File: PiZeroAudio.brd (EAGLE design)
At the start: 65.1 x 30.2 mm, 53 parts, among them CN1 1X4-BIG, CON1 RPI-ZERO, J1 1X2-3.5MM, U3 NC7WZ16, U4 TPA3144D2PWPR

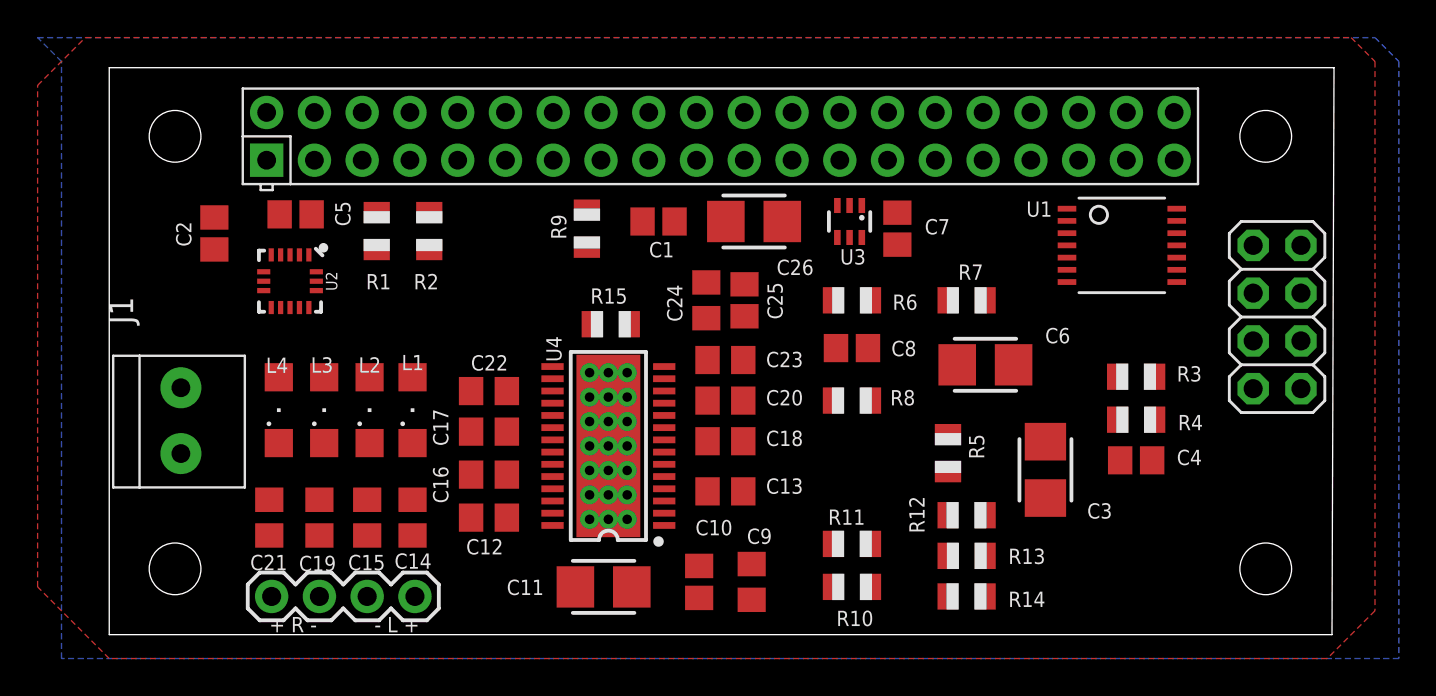
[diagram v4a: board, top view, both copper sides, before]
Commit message: Consistency put back Removed GND pour from top
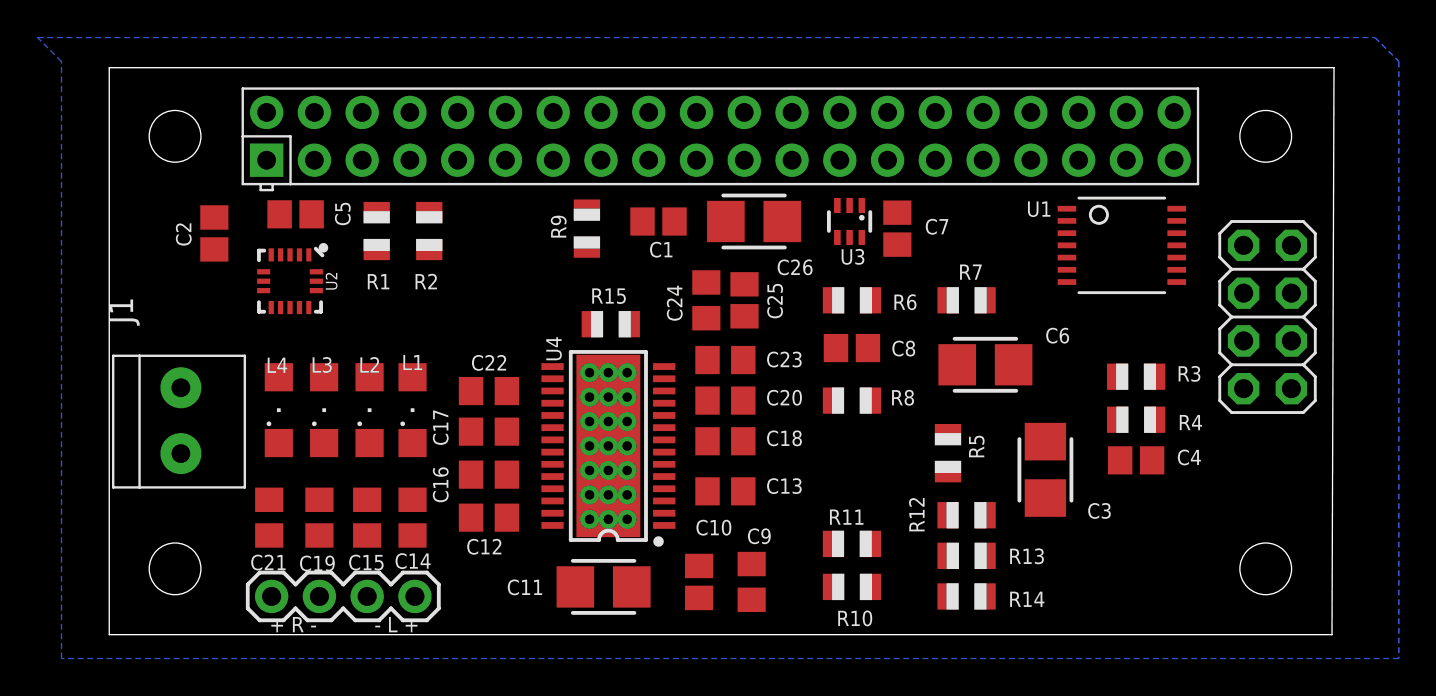
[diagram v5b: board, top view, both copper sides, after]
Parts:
- U1: value (none) -> TXB0104PWR
- U2: value (none) -> LSM6DS33
- moved JP1 0.51 mm to (-17.1, 18.2)
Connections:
- removed net N$6: U4.3
- net AUDIO-L: now also U4.3
- net GND: now also U4.GND@10, U4.GND@11, U4.GND@12, U4.GND@13, U4.GND@14, U4.GND@15, U4.GND@16, U4.GND@17, U4.GND@18, U4.GND@19, U4.GND@20, U4.GND@21, U4.GND@22, U4.GND@23, U4.GND@24, U4.GND@25, U4.GND@26, U4.GND@27, U4.GND@28, U4.GND@29, U4.GND@30, U4.GND@PAD
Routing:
- removed copper zone on layer 1, net GND
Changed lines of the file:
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@@
 <grid distance="50" unitdist="mil" unit="mil" style="lines" multiple="1" display="no" altdistance="5" altunitdist="mil" altunit="mil"/>
 <layers>
-<layer number="1" name="Top" color="4" fill="1" visible="no" active="yes"/>
+<layer number="1" name="Top" color="4" fill="1" visible="yes" active="yes"/>
 <layer number="2" name="Route2" color="16" fill="1" visible="no" active="no"/>
 <layer number="3" name="Route3" color="17" fill="1" visible="no" active="no"/>
@@
 <attribute name="NAME" x="-37.211" y="13.462" size="0.8128" layer="25"/>
 </element>
-<element name="U2" library="HappyBrackets" library_urn="urn:adsk.eagle:library:5224691" package="LGA-16-3X3" package3d_urn="urn:adsk.eagle:package:5224694/1" value="" x="-69.1264" y="20.066" rot="R270"/>
+<element name="U2" library="HappyBrackets" library_urn="urn:adsk.eagle:library:5224691" package="LGA-16-3X3" package3d_urn="urn:adsk.eagle:package:5224694/1" value="LSM6DS33" x="-69.1264" y="20.066" rot="R270"/>
 <element name="C5" library="adafruit" package="C0805" value="100nF" x="-68.8292" y="23.622" smashed="yes">
 <attribute name="NAME" x="-65.913" y="22.987" size="0.8128" layer="25" rot="R90"/>
@@
 <attribute name="NAME" x="-75.184" y="23.241" size="0.8128" layer="25" rot="R270"/>
 </element>
-<element name="U1" library="adafruit" package="TSSOP14" value="" x="-24.892" y="21.971" smashed="yes" rot="R270">
+<element name="U1" library="adafruit" package="TSSOP14" value="TXB0104PWR" x="-24.892" y="21.971" smashed="yes" rot="R270">
 <attribute name="NAME" x="-29.972" y="23.495" size="0.8128" layer="25" ratio="10"/>
-<attribute name="VALUE" x="-26.9748" y="18.0848" size="1.016" layer="27" ratio="10"/>
 </element>
 <element name="CN1" library="adafruit" package="1X04-BIG" value="1X4-BIG" x="-62.484" y="3.302" smashed="yes" rot="R180"/>
@@
 <attribute name="NAME" x="-28.956" y="3.556" size="0.8128" layer="25" rot="R180"/>
 </element>
-<element name="JP1" library="adafruit" package="2X04" value="GPIO" x="-16.637" y="18.161" smashed="yes" rot="R270">
-<attribute name="VALUE" x="-18.796" y="23.368" size="1.27" layer="27"/>
+<element name="JP1" library="adafruit" package="2X04" value="GPIO" x="-17.145" y="18.161" smashed="yes" rot="R270">
+<attribute name="VALUE" x="-19.304" y="23.368" size="1.27" layer="27"/>
 </element>
 </elements>
@@
 <contactref element="JP1" pad="6"/>
 <contactref element="JP1" pad="8"/>
-<polygon width="0.1524" layer="1">
-<vertex x="-80.01" y="33.02"/>
-<vertex x="-12.7" y="33.02"/>
-<vertex x="-11.43" y="31.75"/>
-<vertex x="-11.43" y="2.54"/>
-<vertex x="-13.97" y="0"/>
-<vertex x="-78.74" y="0"/>
-<vertex x="-82.55" y="3.81"/>
-<vertex x="-82.55" y="30.48"/>
-</polygon>
 <polygon width="0.1524" layer="16">
 <vertex x="-82.55" y="33.02"/>
@@
 <vertex x="-81.28" y="31.75"/>
 </polygon>
+<contactref element="U4" pad="GND@10"/>
+<contactref element="U4" pad="GND@11"/>
+<contactref element="U4" pad="GND@12"/>
+<contactref element="U4" pad="GND@13"/>
+<contactref element="U4" pad="GND@14"/>
+<contactref element="U4" pad="GND@15"/>
+<contactref element="U4" pad="GND@16"/>
+<contactref element="U4" pad="GND@17"/>
+<contactref element="U4" pad="GND@18"/>
+<contactref element="U4" pad="GND@19"/>
+<contactref element="U4" pad="GND@20"/>
+<contactref element="U4" pad="GND@21"/>
+<contactref element="U4" pad="GND@22"/>
+<contactref element="U4" pad="GND@23"/>
+<contactref element="U4" pad="GND@24"/>
+<contactref element="U4" pad="GND@25"/>
+<contactref element="U4" pad="GND@26"/>
+<contactref element="U4" pad="GND@27"/>
+<contactref element="U4" pad="GND@28"/>
+<contactref element="U4" pad="GND@29"/>
+<contactref element="U4" pad="GND@30"/>
+<contactref element="U4" pad="GND@PAD"/>
 </signal>
 <signal name="PWM-LEFT">
@@
 <wire x1="-27.19" y1="29.04" x2="-53.34" y2="23.86" width="0" layer="19" extent="1-1"/>
 </signal>
-<signal name="N$6">
-<contactref element="U4" pad="3"/>
-</signal>
 <signal name="N$7">
 <contactref element="U4" pad="4"/>
@@
 <contactref element="U1" pad="13"/>
 <contactref element="JP1" pad="1"/>
-<wire x1="-17.907" y1="21.971" x2="-21.9742" y2="23.271" width="0" layer="19" extent="1-1"/>
+<wire x1="-18.415" y1="21.971" x2="-21.9742" y2="23.271" width="0" layer="19" extent="1-1"/>
 </signal>
 <signal name="N$12">
 <contactref element="U1" pad="12"/>
 <contactref element="JP1" pad="3"/>
-<wire x1="-17.907" y1="19.431" x2="-21.9742" y2="22.621" width="0" layer="19" extent="1-1"/>
+<wire x1="-18.415" y1="19.431" x2="-21.9742" y2="22.621" width="0" layer="19" extent="1-1"/>
 </signal>
 <signal name="N$14">
 <contactref element="U1" pad="11"/>
 <contactref element="JP1" pad="5"/>
-<wire x1="-21.9742" y1="21.971" x2="-17.907" y2="16.891" width="0" layer="19" extent="1-1"/>
+<wire x1="-21.9742" y1="21.971" x2="-18.415" y2="16.891" width="0" layer="19" extent="1-1"/>
 </signal>
 <signal name="N$15">
 <contactref element="U1" pad="10"/>
 <contactref element="JP1" pad="7"/>
-<wire x1="-21.9742" y1="21.321" x2="-17.907" y2="14.351" width="0" layer="19" extent="1-1"/>
+<wire x1="-21.9742" y1="21.321" x2="-18.415" y2="14.351" width="0" layer="19" extent="1-1"/>
 </signal>
 <signal name="GPIO23">
@@
 <contactref element="C6" pad="-"/>
 <contactref element="R8" pad="2"/>
+<contactref element="U4" pad="3"/>
+<wire x1="-38.243" y1="13.716" x2="-49.227" y2="8.378" width="0" layer="19" extent="1-1"/>
 <wire x1="-33.647" y1="15.621" x2="-38.243" y2="13.716" width="0" layer="19" extent="1-1"/>
 </signal>
@@
 <mfgpreviewcolor name="substratecolor" color="0xFF786E46"/>
 </mfgpreviewcolors>
+<errors>
+</errors>
 </board>
 </drawing>

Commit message: Applied star Power
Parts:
- added SH1, SH2: SHORT, HappyBrackets:SHORT
- moved C1 20.1 mm to (-29.5, 23.0), turned to 270 degrees
- moved U3 0.64 mm to (-39.9, 23.6)
- moved U1 0.63 mm to (-24.4, 22.4)
- moved C2 0.18 mm to (-73.3, 22.5), turned to 90 degrees
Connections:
- new net AGND: C10.2, C11.-, C13.2, C14.2, C15.1, C18.2, C19.2, C20.2, C21.1, C23.2, C24.2, C25.2, C26.-, C4.2, C7.2, C8.2, C9.2, J1.1, R10.2, R12.2, R4.1, R5.1, R7.1, R8.1, SH2.AN, U4.10, U4.13, U4.19, U4.24
- new net AN3V3: C7.1, SH1.AN, U3.5
- net +3V3: now also SH1.DIG; no longer C7.1, U3.5
- net GND: now also SH2.DIG; no longer C10.2, C11.-, C13.2, C14.2, C15.1, C18.2, C19.2, C20.2, C21.1, C23.2, C24.2, C25.2, C26.-, C4.2, C7.2, C8.2, C9.2, J1.1, R10.2, R12.2, R4.1, R5.1, R7.1, R8.1, U4.10, U4.13, U4.19, U4.24
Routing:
- added copper zone on layer 1, net +3V3
- added copper zone on layer 1, net +5V
- added copper zone on layer 1, net AN3V3
- added copper zone on layer 16, net ANGND

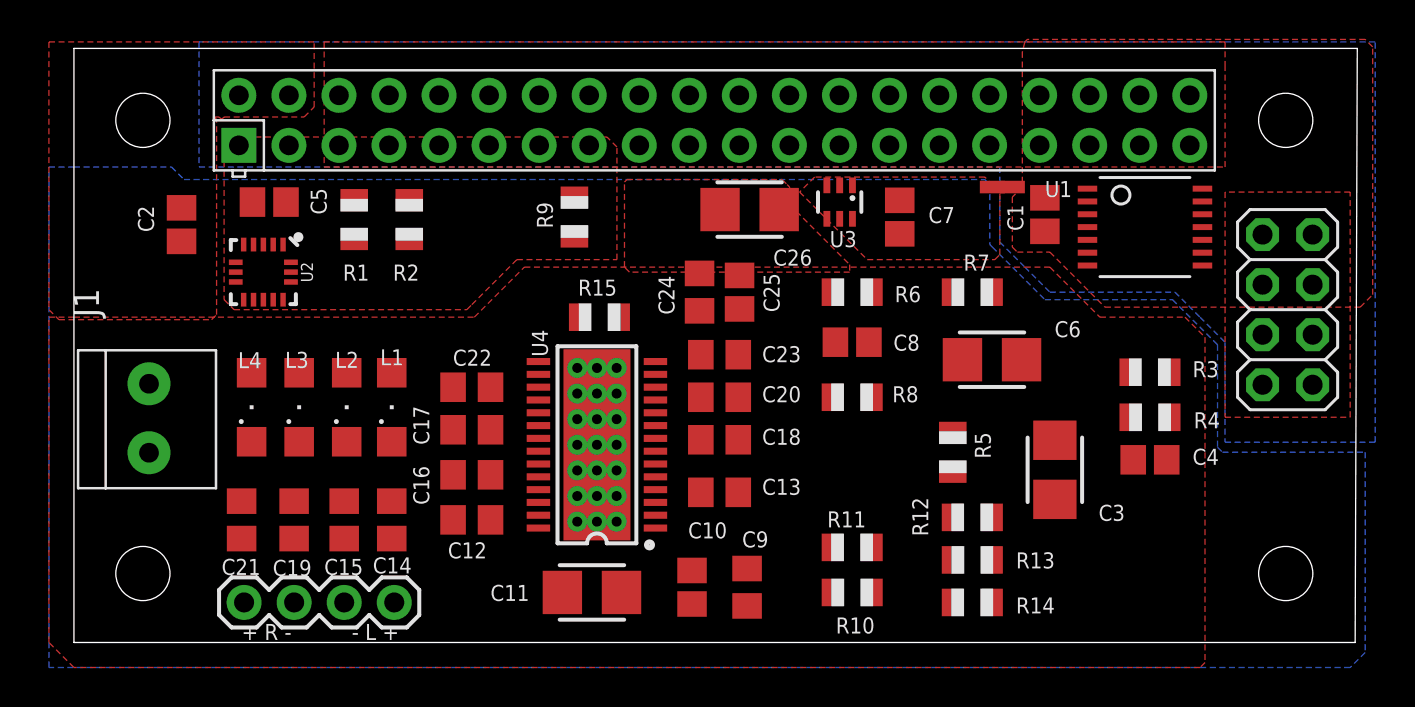
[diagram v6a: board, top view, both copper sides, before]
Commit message: Changed Ferrite Beads
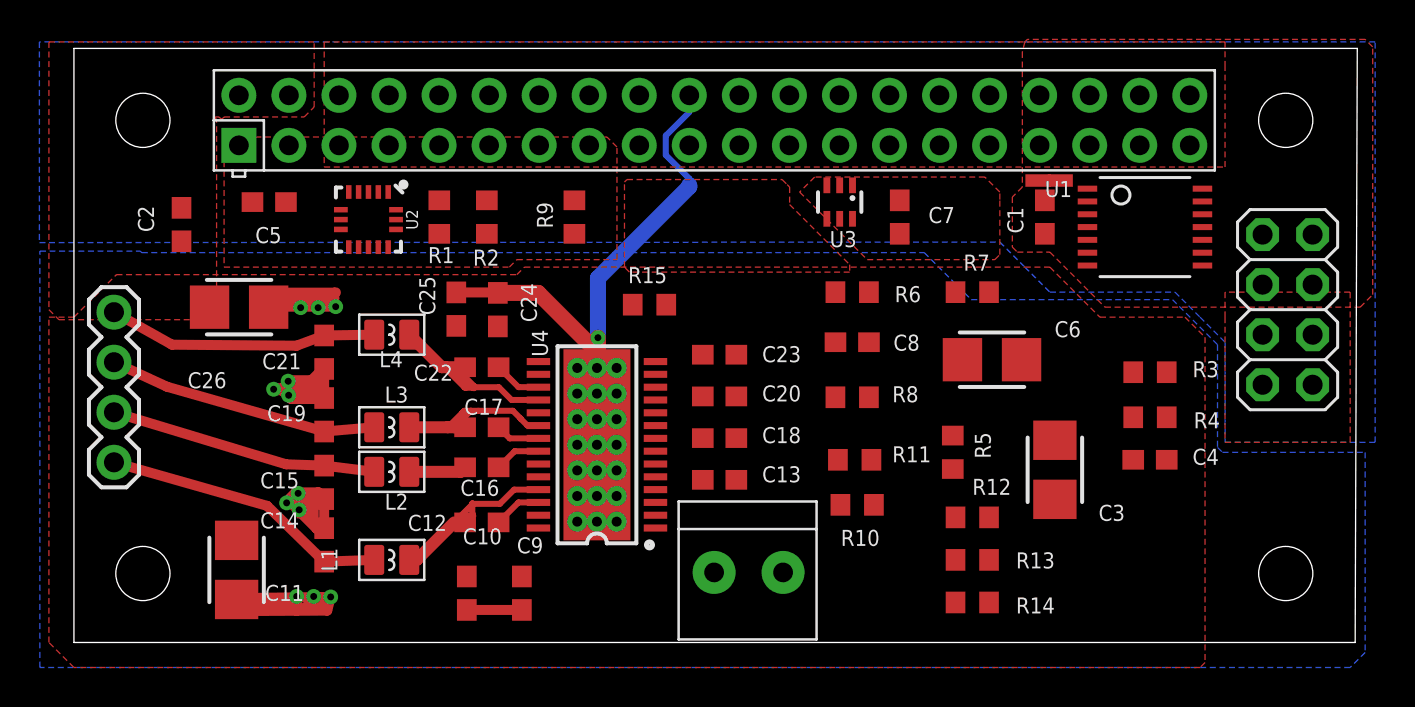
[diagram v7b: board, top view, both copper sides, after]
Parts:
- C1, C10, C2, C25, C4, C5, C7, C8: device adafruit:C0805 -> rcl:C0603
- C12, C13, C14, C15, C16, C17, C18, C19, C20, C21, C22, C23, C24, C9: device resistor:C0805 -> rcl:C0603
- L1, L2, L3, L4: device HappyBrackets:SML1206 -> HappyBrackets:L0806
- R1, R10, R11, R12, R13, R14, R15, R2, R3, R4, R5, R6, R7, R8, R9: device adafruit:R0805 -> adafruit:R0603
- moved J1 31.5 mm to (-44.5, 4.83), turned to 180 degrees
- moved C26 26.4 mm to (-70.4, 18.3)
- moved C11 18.1 mm to (-70.5, 4.95), turned to 90 degrees
- moved CN1 15.9 mm to (-76.7, 10.4), turned to 90 degrees
- moved C25 14.4 mm to (-59.3, 18.2)
- moved C10 11.4 mm to (-58.8, 3.77)
- moved C9 11.4 mm to (-56.0, 3.77)
- moved C24 10.3 mm to (-57.2, 18.2)
- moved C21 9.49 mm to (-66.0, 16.0), turned to 90 degrees
- moved L4 8.01 mm to (-62.6, 16.9), turned to 180 degrees
- moved L1 7.75 mm to (-62.6, 5.46), turned to 180 degrees
- moved U2 5.96 mm to (-63.8, 22.7)
- moved C19 5.55 mm to (-66.0, 12.8)
- moved L3 4.81 mm to (-62.6, 12.2), turned to 180 degrees
- moved SH2 4.57 mm to (-52.2, 15.1), turned to 90 degrees
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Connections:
- net AGND: now also U4.GND@10, U4.GND@11, U4.GND@12, U4.GND@13, U4.GND@14, U4.GND@15, U4.GND@16, U4.GND@17, U4.GND@18, U4.GND@19, U4.GND@20, U4.GND@21, U4.GND@22, U4.GND@23, U4.GND@24, U4.GND@25, U4.GND@26, U4.GND@27, U4.GND@28, U4.GND@29, U4.GND@30, U4.GND@PAD
- net GND: no longer U4.GND@10, U4.GND@11, U4.GND@12, U4.GND@13, U4.GND@14, U4.GND@15, U4.GND@16, U4.GND@17, U4.GND@18, U4.GND@19, U4.GND@20, U4.GND@21, U4.GND@22, U4.GND@23, U4.GND@24, U4.GND@25, U4.GND@26, U4.GND@27, U4.GND@28, U4.GND@29, U4.GND@30, U4.GND@PAD
- net L+: now also L1.2; no longer L1.C
- net L-: now also L2.2; no longer L2.C
- net N$18: now also L1.1; no longer L1.A
- net N$19: now also L2.1; no longer L2.A
- net N$20: now also L3.1; no longer L3.A
- net N$21: now also L4.1; no longer L4.A
- net R+: now also L4.2; no longer L4.C
- net R-: now also L3.2; no longer L3.C
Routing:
- net AGND: track 0.00 -> 49.2 mm, vias 0 -> 12
- net GND: track 0.00 -> 16.4 mm, vias 0 -> 1
- net L+: track 0.00 -> 14.7 mm
- net R-: track 0.00 -> 13.8 mm
- net R+: track 0.00 -> 13.7 mm
- net L-: track 0.00 -> 13.6 mm
- net N$21: track 0.00 -> 10.1 mm
- net N$20: track 0.00 -> 9.28 mm
- net N$18: track 0.00 -> 8.72 mm
- net N$19: track 0.00 -> 2.93 mm
- net N$17: track 0.00 -> 2.44 mm
- net N$10: track 0.00 -> 2.44 mm
- net N$16: track 0.00 -> 2.36 mm
- net N$13: track 0.00 -> 2.26 mm
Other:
- board text removed: "+ R -"
- board text removed: "- L +"

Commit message: Routed all but power
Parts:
- moved R1 7.35 mm to (-67.5, 23.3)
- moved SH1 3.13 mm to (-32.3, 24.3)
- moved C1 2.92 mm to (-32.4, 23.0)
- moved R2 2.26 mm to (-60.0, 22.9)
- moved C5 1.55 mm to (-70.4, 23.6)
- moved C3 0.95 mm to (-29.0, 11.0), turned to 0 degrees
- moved U3 0.71 mm to (-39.9, 22.9)
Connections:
- net PWM-LEFT renamed PWM-R
- net PWM-RIGHT renamed PWM-L
- removed net AUDIO-L: C6.-, R8.2, U4.3
- removed net AUDIO-R: C3.-, R5.2, U4.12
- new net AUDIO-LEFT: C3.-, R5.2, U4.3
- new net AUDIO-RIGHT: C6.-, R8.2, U4.12
- net GPIO21: now also U1.5; no longer U1.2
- net GPIO22: now also U1.4; no longer U1.3
- net GPIO23: now also U1.3; no longer U1.4
- net GPIO25: now also U1.2; no longer U1.5
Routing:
- net AGND: track 49.2 -> 78.1 mm
- net N$26: track 0.00 -> 28.5 mm
- net AUDIO-LEFT: track 0.00 -> 22.9 mm, vias 0 -> 2
- net N$24: track 0.00 -> 22.8 mm, vias 0 -> 2
- net PWM-R: track 0.00 -> 20.7 mm
- net N$2: track 0.00 -> 20.3 mm
- net AUDIO-RIGHT: track 0.00 -> 19.3 mm, vias 0 -> 2
- net N$23: track 0.00 -> 18.7 mm, vias 0 -> 2
- net N$25: track 0.00 -> 14.6 mm
- net ACC-INT2: track 0.00 -> 13.5 mm, vias 0 -> 1
- net PWM-L: track 0.00 -> 13.3 mm, vias 0 -> 1
- net N$4: track 0.00 -> 12.0 mm
- net ACC-INT1: track 0.00 -> 10.9 mm, vias 0 -> 1
- net GPIO21: track 0.00 -> 9.94 mm
- net N$15: track 0.00 -> 9.10 mm
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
